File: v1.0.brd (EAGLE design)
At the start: 160 x 100 mm, 106 parts, among them J1 DC-044-A, J2 MICROSD-9P, J3 2p-2.54, J4 2p-2.54, Q1 SI4532ADY, Q3 6pF@32.7680kHz, U1 MCP23017-E/SO, U10 74HC139N, U2 MCP79412-I/SN, U3 LOPY, U4 GROVE_DC&DC, U5 LM1085IT-5.0, U6 FT232RL-SSOP28, U7 2x14p-2.54, U8 FT232RL-SSOP28, U9 SP483ECN-L, X1 JST-XH-05-PIN-ROUND-PAD, X10 JST-XH-07-PIN-ROUND-PAD, X11 JST-XH-07-PIN-ROUND-PAD, X12 JST-XH-07-PIN-ROUND-PAD, X13 JST-XH-05-PIN-ROUND-PAD, X14 JST-XH-05-PIN-ROUND-PAD, X15 JST-XH-05-PIN-ROUND-PAD, X16 JST-XH-05-PIN-ROUND-PAD, X17 JST-XH-05-PIN-ROUND-PAD, X18 JST-XH-05-PIN-ROUND-PAD, X19 JST-XH-05-PIN-ROUND-PAD, X2 JST-XH-05-PIN-ROUND-PAD, X20 JST-XH-05-PIN-ROUND-PAD, X21 JST-XH-05-PIN-ROUND-PAD, X22 JST-XH-05-PIN-ROUND-PAD, X23 JST-XH-05-PIN-ROUND-PAD, X3 JST-XH-05-PIN-ROUND-PAD, X4 JST-XH-07-PIN-ROUND-PAD, X5 JST-XH-07-PIN-ROUND-PAD, X6 JST-XH-07-PIN-ROUND-PAD, X7 JST-XH-07-PIN-ROUND-PAD, X8 JST-XH-07-PIN-ROUND-PAD, X9 JST-XH-07-PIN-ROUND-PAD

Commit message: adc sockets
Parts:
- added X24, X25, X26, X27: JST-XH-07-PIN-ROUND-PAD, Rembrandt Electronics - JST XH Connectors v1-0 2:JST-XH-07-PACKAGE-ROUND-PAD
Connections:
- removed net N$13: U$1.2
- removed net N$14: U$1.3
- removed net N$15: U$1.4
- removed net N$16: U$1.11
- removed net N$19: U$1.1
- removed net N$22: U$2.1
- removed net N$24: U$1.12
- removed net N$26: U$1.13
- removed net N$27: U$1.14
- removed net N$35: U$2.2
- removed net N$36: U$2.3
- removed net N$39: U$2.4
- removed net N$40: U$2.11
- removed net N$41: U$2.12
- removed net N$42: U$2.13
- removed net N$44: U$2.14
- new net ADC1+: U$1.1, X27.4
- new net ADC1-: U$1.2, X27.5
- new net ADC2+: U$1.3, X27.6
- new net ADC2-: U$1.4, X27.7
- new net ADC3+: U$1.11, X24.4
- new net ADC3-: U$1.12, X24.5
- new net ADC4+: U$1.13, X24.6
- new net ADC4-: U$1.14, X24.7
- new net ADC5+: U$2.1, X25.4
- new net ADC5-: U$2.2, X25.5
- new net ADC6+: U$2.3, X25.6
- new net ADC6-: U$2.4, X25.7
- new net ADC7+: U$2.11, X26.4
- new net ADC7-: U$2.12, X26.5
- new net ADC8+: U$2.13, X26.6
- new net ADC8-: U$2.14, X26.7
- net 3V3_SMOOTH: now also X24.2, X25.2, X26.2, X27.2
- net GND: now also X24.3, X25.3, X26.3, X27.3
- net PI_5V: now also X24.1, X25.1, X26.1, X27.1
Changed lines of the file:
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@@
 <element name="X21" library="Rembrandt Electronics - JST XH Connectors v1-0 2" package="JST-XH-05-PACKAGE-ROUND-PAD" value="JST-XH-05-PIN-ROUND-PAD" x="-134.62" y="-118.11"/>
 <element name="X22" library="Rembrandt Electronics - JST XH Connectors v1-0 2" package="JST-XH-05-PACKAGE-ROUND-PAD" value="JST-XH-05-PIN-ROUND-PAD" x="-134.62" y="-133.35"/>
+<element name="X27" library="Rembrandt Electronics - JST XH Connectors v1-0 2" package="JST-XH-07-PACKAGE-ROUND-PAD" value="JST-XH-07-PIN-ROUND-PAD" x="-132.08" y="-194.31"/>
+<element name="X24" library="Rembrandt Electronics - JST XH Connectors v1-0 2" package="JST-XH-07-PACKAGE-ROUND-PAD" value="JST-XH-07-PIN-ROUND-PAD" x="-132.08" y="-209.55"/>
+<element name="X25" library="Rembrandt Electronics - JST XH Connectors v1-0 2" package="JST-XH-07-PACKAGE-ROUND-PAD" value="JST-XH-07-PIN-ROUND-PAD" x="-132.08" y="-224.79"/>
+<element name="X26" library="Rembrandt Electronics - JST XH Connectors v1-0 2" package="JST-XH-07-PACKAGE-ROUND-PAD" value="JST-XH-07-PIN-ROUND-PAD" x="-132.08" y="-240.03"/>
 </elements>
 <signals>
@@
 <contactref element="X21" pad="3"/>
 <contactref element="X22" pad="3"/>
+<contactref element="X27" pad="3"/>
+<contactref element="X24" pad="3"/>
+<contactref element="X25" pad="3"/>
+<contactref element="X26" pad="3"/>
 <wire x1="-134.62" y1="-102.87" x2="-134.62" y2="-118.11" width="0" layer="19" extent="1-1"/>
 <wire x1="-134.62" y1="-87.63" x2="-134.62" y2="-102.87" width="0" layer="19" extent="1-1"/>
@@
 <wire x1="-15.24" y1="158.369" x2="-15.24" y2="163.322" width="0" layer="19" extent="1-1"/>
 <wire x1="-86.36" y1="156.718" x2="-106.68" y2="155.448" width="0" layer="19" extent="1-1"/>
+<wire x1="-134.62" y1="-194.31" x2="-134.62" y2="-133.35" width="0" layer="19" extent="1-1"/>
+<wire x1="-134.62" y1="-209.55" x2="-134.62" y2="-194.31" width="0" layer="19" extent="1-1"/>
+<wire x1="-134.62" y1="-224.79" x2="-134.62" y2="-209.55" width="0" layer="19" extent="1-1"/>
+<wire x1="-134.62" y1="-240.03" x2="-134.62" y2="-224.79" width="0" layer="19" extent="1-1"/>
 </signal>
 <signal name="+3V3">
@@
 <contactref element="X22" pad="1"/>
 <contactref element="X23" pad="1"/>
+<contactref element="X27" pad="1"/>
+<contactref element="X24" pad="1"/>
+<contactref element="X25" pad="1"/>
+<contactref element="X26" pad="1"/>
 <wire x1="-139.7" y1="-87.63" x2="-139.7" y2="-102.87" width="0" layer="19" extent="1-1"/>
 <wire x1="-139.7" y1="-72.39" x2="-139.7" y2="-87.63" width="0" layer="19" extent="1-1"/>
@@
 <wire x1="-40.7162" y1="93.345" x2="-30.48" y2="116.84" width="0" layer="19" extent="1-1"/>
 <wire x1="-20.32" y1="156.591" x2="-45.72" y2="161.798" width="0" layer="19" extent="1-1"/>
+<wire x1="-139.7" y1="-194.31" x2="-139.7" y2="-133.35" width="0" layer="19" extent="1-1"/>
+<wire x1="-139.7" y1="-209.55" x2="-139.7" y2="-194.31" width="0" layer="19" extent="1-1"/>
+<wire x1="-139.7" y1="-224.79" x2="-139.7" y2="-209.55" width="0" layer="19" extent="1-1"/>
+<wire x1="-139.7" y1="-240.03" x2="-139.7" y2="-224.79" width="0" layer="19" extent="1-1"/>
 </signal>
 <signal name="N$1">
@@
 <contactref element="X22" pad="2"/>
 <contactref element="X23" pad="2"/>
+<contactref element="X27" pad="2"/>
+<contactref element="X24" pad="2"/>
+<contactref element="X25" pad="2"/>
+<contactref element="X26" pad="2"/>
 <wire x1="-137.16" y1="-87.63" x2="-137.16" y2="-102.87" width="0" layer="19" extent="1-1"/>
 <wire x1="-137.16" y1="-72.39" x2="-137.16" y2="-87.63" width="0" layer="19" extent="1-1"/>
@@
 <wire x1="-137.16" y1="-118.11" x2="-137.16" y2="-102.87" width="0" layer="19" extent="1-1"/>
 <wire x1="-137.16" y1="-133.35" x2="-137.16" y2="-118.11" width="0" layer="19" extent="1-1"/>
+<wire x1="-137.16" y1="-194.31" x2="-137.16" y2="-133.35" width="0" layer="19" extent="1-1"/>
+<wire x1="-137.16" y1="-209.55" x2="-137.16" y2="-194.31" width="0" layer="19" extent="1-1"/>
+<wire x1="-137.16" y1="-224.79" x2="-137.16" y2="-209.55" width="0" layer="19" extent="1-1"/>
+<wire x1="-137.16" y1="-240.03" x2="-137.16" y2="-224.79" width="0" layer="19" extent="1-1"/>
 <wire x1="-120.65" y1="104.14" x2="-137.16" y2="-11.43" width="0" layer="19" extent="1-1"/>
 <wire x1="-119.38" y1="116.84" x2="-120.65" y2="104.14" width="0" layer="19" extent="1-1"/>
@@
 <wire x1="-104.14" y1="143.002" x2="-17.145" y2="102.81" width="0" layer="19" extent="1-1"/>
 </signal>
-<signal name="N$13">
+<signal name="ADC1-">
 <contactref element="U$1" pad="2"/>
-</signal>
-<signal name="N$14">
+<contactref element="X27" pad="5"/>
+<wire x1="-109.0422" y1="71.12" x2="-129.54" y2="-194.31" width="0" layer="19" extent="1-1"/>
+</signal>
+<signal name="ADC2+">
 <contactref element="U$1" pad="3"/>
-</signal>
-<signal name="N$15">
+<contactref element="X27" pad="6"/>
+<wire x1="-109.0422" y1="69.85" x2="-127" y2="-194.31" width="0" layer="19" extent="1-1"/>
+</signal>
+<signal name="ADC2-">
 <contactref element="U$1" pad="4"/>
-</signal>
-<signal name="N$16">
+<contactref element="X27" pad="7"/>
+<wire x1="-109.0422" y1="68.58" x2="-124.46" y2="-194.31" width="0" layer="19" extent="1-1"/>
+</signal>
+<signal name="ADC3+">
 <contactref element="U$1" pad="11"/>
+<contactref element="X24" pad="4"/>
+<wire x1="-104.3178" y1="68.58" x2="-132.08" y2="-209.55" width="0" layer="19" extent="1-1"/>
 </signal>
 <signal name="+3V3_SMOOTH">
@@
 <wire x1="-109.0422" y1="66.04" x2="-130.6322" y2="66.04" width="0" layer="19" extent="1-1"/>
 </signal>
-<signal name="N$19">
-<contactref element="U$1" pad="1"/>
-</signal>
-<signal name="N$24">
+<signal name="ADC3-">
 <contactref element="U$1" pad="12"/>
-</signal>
-<signal name="N$26">
+<contactref element="X24" pad="5"/>
+<wire x1="-104.3178" y1="69.85" x2="-129.54" y2="-209.55" width="0" layer="19" extent="1-1"/>
+</signal>
+<signal name="ADC4+">
 <contactref element="U$1" pad="13"/>
-</signal>
-<signal name="N$27">
+<contactref element="X24" pad="6"/>
+<wire x1="-104.3178" y1="71.12" x2="-127" y2="-209.55" width="0" layer="19" extent="1-1"/>
+</signal>
+<signal name="ADC4-">
 <contactref element="U$1" pad="14"/>
-</signal>
-<signal name="N$22">
+<contactref element="X24" pad="7"/>
+<wire x1="-104.3178" y1="72.39" x2="-124.46" y2="-209.55" width="0" layer="19" extent="1-1"/>
+</signal>
+<signal name="ADC5+">
 <contactref element="U$2" pad="1"/>
-</signal>
-<signal name="N$35">
+<contactref element="X25" pad="4"/>
+<wire x1="-130.6322" y1="72.39" x2="-132.08" y2="-224.79" width="0" layer="19" extent="1-1"/>
+</signal>
+<signal name="ADC5-">
 <contactref element="U$2" pad="2"/>
-</signal>
-<signal name="N$36">
+<contactref element="X25" pad="5"/>
+<wire x1="-130.6322" y1="71.12" x2="-129.54" y2="-224.79" width="0" layer="19" extent="1-1"/>
+</signal>
+<signal name="ADC6+">
 <contactref element="U$2" pad="3"/>
-</signal>
-<signal name="N$39">
+<contactref element="X25" pad="6"/>
+<wire x1="-130.6322" y1="69.85" x2="-127" y2="-224.79" width="0" layer="19" extent="1-1"/>
+</signal>
+<signal name="ADC6-">
 <contactref element="U$2" pad="4"/>
-</signal>
-<signal name="N$40">
+<contactref element="X25" pad="7"/>
+<wire x1="-130.6322" y1="68.58" x2="-124.46" y2="-224.79" width="0" layer="19" extent="1-1"/>
+</signal>
+<signal name="ADC7+">
 <contactref element="U$2" pad="11"/>
-</signal>
-<signal name="N$41">
-<contactref element="U$2" pad="12"/>
-</signal>
-<signal name="N$42">
+<contactref element="X26" pad="4"/>
+<wire x1="-125.9078" y1="68.58" x2="-132.08" y2="-240.03" width="0" layer="19" extent="1-1"/>
+</signal>
+<signal name="ADC8+">
 <contactref element="U$2" pad="13"/>
-</signal>
-<signal name="N$44">
+<contactref element="X26" pad="6"/>
+<wire x1="-125.9078" y1="71.12" x2="-127" y2="-240.03" width="0" layer="19" extent="1-1"/>
+</signal>
+<signal name="ADC8-">
 <contactref element="U$2" pad="14"/>
+<contactref element="X26" pad="7"/>
+<wire x1="-125.9078" y1="72.39" x2="-124.46" y2="-240.03" width="0" layer="19" extent="1-1"/>
 </signal>
 <signal name="N$23">
@@
 <wire x1="-45.6438" y1="92.075" x2="-64.355" y2="86.545" width="0" layer="19" extent="1-1"/>
 </signal>
+<signal name="ADC7-">
+<contactref element="X26" pad="5"/>
+<contactref element="U$2" pad="12"/>
+<wire x1="-125.9078" y1="69.85" x2="-129.54" y2="-240.03" width="0" layer="19" extent="1-1"/>
+</signal>
+<signal name="ADC1+">
+<contactref element="U$1" pad="1"/>
+<contactref element="X27" pad="4"/>
+<wire x1="-109.0422" y1="72.39" x2="-132.08" y2="-194.31" width="0" layer="19" extent="1-1"/>
+</signal>
 </signals>

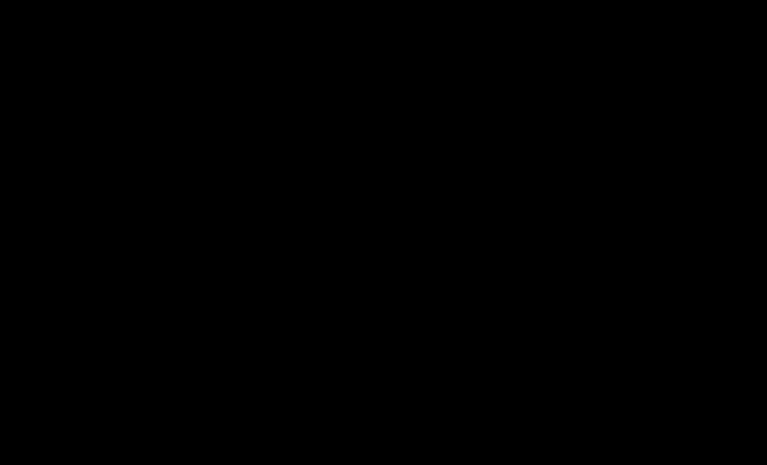
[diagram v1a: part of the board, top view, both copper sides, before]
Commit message: changed back to +5V - has LDO on it - and added RS485 socket
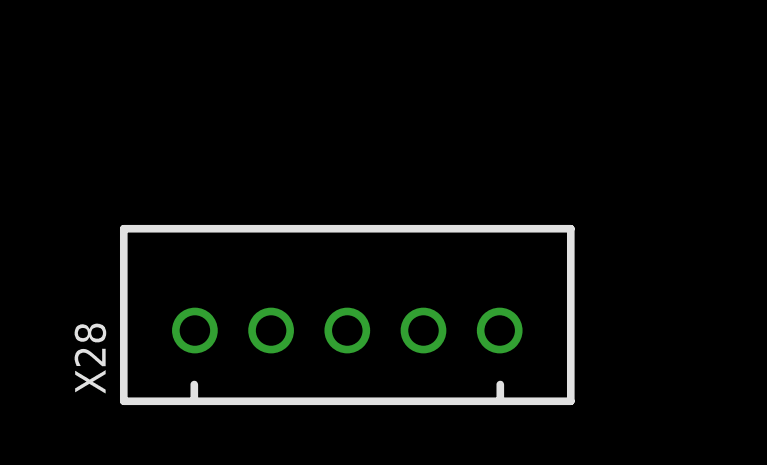
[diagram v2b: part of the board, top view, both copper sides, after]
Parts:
- added X28: JST-XH-05-PIN-ROUND-PAD, Rembrandt Electronics - JST XH Connectors v1-0 2:JST-XH-05-PACKAGE-ROUND-PAD
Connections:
- net +5V: now also X10.1, X11.1, X12.1, X13.1, X14.1, X15.1, X16.1, X17.1, X18.1, X19.1, X20.1, X21.1, X22.1, X23.1, X24.1, X25.1, X26.1, X27.1, X28.1, X5.1, X6.1, X7.1, X8.1, X9.1
- net 3V3_SMOOTH: now also X28.2
- net GND: now also X28.3
- net PI_5V: no longer X10.1, X11.1, X12.1, X13.1, X14.1, X15.1, X16.1, X17.1, X18.1, X19.1, X20.1, X21.1, X22.1, X23.1, X24.1, X25.1, X26.1, X27.1, X5.1, X6.1, X7.1, X8.1, X9.1
- net RS485_A: now also X28.4
- net RS485_B: now also X28.5

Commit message: zener diode
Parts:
- added U11: BZX84C30, Diodes_Inc_By_element14_Batch_1:SOT91P240X110-3N
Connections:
- net +24V: now also U11.1
- net GND: now also U11.3
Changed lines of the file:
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@@
 <element name="X26" library="Rembrandt Electronics - JST XH Connectors v1-0 2" package="JST-XH-07-PACKAGE-ROUND-PAD" value="JST-XH-07-PIN-ROUND-PAD" x="-132.08" y="-240.03"/>
 <element name="X28" library="Rembrandt Electronics - JST XH Connectors v1-0 2" package="JST-XH-05-PACKAGE-ROUND-PAD" value="JST-XH-05-PIN-ROUND-PAD" x="-134.62" y="-255.27"/>
+<element name="U11" library="Diodes_Inc_By_element14_Batch_1" package="SOT91P240X110-3N" value="BZX84C30" x="-143.51" y="-269.24">
+<attribute name="MPN" value="BZX84C30" x="-143.51" y="-269.24" size="1.778" layer="27" display="off"/>
+<attribute name="OC_FARNELL" value="1902456" x="-143.51" y="-269.24" size="1.778" layer="27" display="off"/>
+<attribute name="OC_NEWARK" value="-" x="-143.51" y="-269.24" size="1.778" layer="27" display="off"/>
+<attribute name="PACKAGE" value="SOT-23-3" x="-143.51" y="-269.24" size="1.778" layer="27" display="off"/>
+<attribute name="SUPPLIER" value="DIODES INC." x="-143.51" y="-269.24" size="1.778" layer="27" display="off"/>
+</element>
 </elements>
 <signals>
@@
 <contactref element="X26" pad="3"/>
 <contactref element="X28" pad="3"/>
+<contactref element="U11" pad="3"/>
 <wire x1="-134.62" y1="-102.87" x2="-134.62" y2="-118.11" width="0" layer="19" extent="1-1"/>
 <wire x1="-134.62" y1="-87.63" x2="-134.62" y2="-102.87" width="0" layer="19" extent="1-1"/>
@@
 <wire x1="-134.62" y1="-240.03" x2="-134.62" y2="-224.79" width="0" layer="19" extent="1-1"/>
 <wire x1="-134.62" y1="-255.27" x2="-134.62" y2="-240.03" width="0" layer="19" extent="1-1"/>
+<wire x1="-142.494" y1="-269.24" x2="-134.62" y2="-255.27" width="0" layer="19" extent="1-1"/>
 </signal>
 <signal name="+3V3">
@@
 <contactref element="U4" pad="P$1"/>
 <contactref element="R5" pad="2"/>
-<wire x1="-95.58" y1="143.51" x2="-40.64" y2="156.718" width="0" layer="19" extent="1-1"/>
-<wire x1="-73.66" y1="74.93" x2="-95.58" y2="143.51" width="0" layer="19" extent="1-1"/>
-<wire x1="-73.66" y1="72.39" x2="-73.66" y2="74.93" width="0" layer="19" extent="1-1"/>
+<contactref element="U11" pad="1"/>
+<wire x1="-73.66" y1="72.39" x2="-144.526" y2="-268.3256" width="0" layer="19" extent="1-1"/>
+<wire x1="-73.66" y1="74.93" x2="-73.66" y2="72.39" width="0" layer="19" extent="1-1"/>
+<wire x1="-95.58" y1="143.51" x2="-73.66" y2="74.93" width="0" layer="19" extent="1-1"/>
+<wire x1="-40.64" y1="156.718" x2="-95.58" y2="143.51" width="0" layer="19" extent="1-1"/>
 </signal>
 <signal name="3V3_SMOOTH">

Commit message: polyfuses
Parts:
- added F10, F100, F101, F102, F103, F104, F105, F106, F107, F108, F109, F11, F110, F111, F112, F113, F114, F115, F116, F117, F118, F119, F12, F120, F121, F122, F123, F13, F14, F15, F16, F17, F18, F19, F2, F20, F21, F22, F23, F24, F25, F26, F27, F28, F29, F3, F30, F31, F32, F33, F34, F35, F36, F37, F38, F39, F4, F40, F41, F42, F43, F44, F45, F46, F47, F48, F49, F5, F50, F51, F52, F53, F54, F55, F56, F57, F58, F59, F6, F60, F61, F62, F63, F64, F65, F66, F67, F68, F69, F7, F70, F71, F72, F73, F74, F75, F76, F77, F78, F79, F8, F80, F81, F82, F83, F84, F85, F86, F87, F88, F89, F9, F90, F91, F92, F93, F94, F95, F96, F97, F98, F99: SMD1206R500SF, Seeed-Fuse:F1206
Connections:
- new net N$12: F109.1, U1.22
- new net N$13: F110.1, U1.23
- new net N$14: F111.1, U1.24
- new net N$15: F112.1, U1.25
- new net N$16: F113.1, U1.26
- new net N$19: F114.1, U1.27
- new net N$2: F106.1, U1.19
- new net N$22: F115.1, U1.28
- new net N$24: F116.1, U1.1
- new net N$26: F117.1, U1.2
- new net N$27: F118.1, U1.3
- new net N$3: F107.1, U1.20
- new net N$35: F119.1, U1.4
- new net N$36: F120.1, U1.5
- new net N$37: F121.1, U1.6
- new net N$39: F122.1, U1.7
- new net N$40: F123.1, U1.8
- new net N$8: F108.1, U1.21
- net ADC1+: now also F54.2
- net ADC1-: now also F55.2
- net ADC2+: now also F56.2
- net ADC2-: now also F57.2
- net ADC3+: now also F58.2
- net ADC3-: now also F59.2
- net ADC4+: now also F60.2
- net ADC4-: now also F61.2
- net ADC5+: now also F62.2
- net ADC5-: now also F63.2
- net ADC6+: now also F64.2
- net ADC6-: now also F65.2
- net ADC7+: now also F66.2
- net ADC7-: now also F67.2
- net ADC8+: now also F68.2
- net ADC8-: now also F69.2
- net LOPY_CS: now also F74.2
- net LOPY_MISO: now also F76.2
- net LOPY_MOSI: now also F77.2
- net LOPY_P13: now also F94.2, F95.1
- net LOPY_P14: now also F93.2, F96.1
- net LOPY_P15: now also F92.2, F97.1
- net LOPY_P16: now also F91.2, F98.1
- net LOPY_P17: now also F90.2, F99.1
- net LOPY_P18: now also F100.1, F89.2
- net LOPY_P19: now also F101.1, F88.2
- net LOPY_P20: now also F102.1, F87.2
- net LOPY_P21: now also F103.1, F86.2
- net LOPY_P22: now also F104.1, F85.2
- net LOPY_P23: now also F105.1, F84.2
- net LOPY_RX0: now also F83.2
- net LOPY_RX1: now also F81.2
- net LOPY_SCL/CLK: now also F75.2, F78.2
- net LOPY_SDA: now also F79.2
- net LOPY_TX0: now also F82.2
- net LOPY_TX1: now also F80.2
- net RPI_CS1: now also F28.2
- net RPI_CS2: now also F29.2
- net RPI_CS3: now also F33.2
- net RPI_CS4: now also F37.2
- net RPI_CS5: now also F41.2
- net RPI_CS6: now also F45.2
- net RPI_CS7: now also F49.2
- net RPI_CS8: now also F53.2
- net RS485_A: now also F72.2
- net RS485_B: now also F73.2
- net SCL_3V3: now also F11.2, F13.2, F15.2, F17.2, F19.2, F21.2, F3.2, F5.2, F6.2, F9.2
- net SDA_3V3: now also F10.2, F12.2, F14.2, F16.2, F18.2, F2.2, F20.2, F4.2, F7.2, F8.2
- net SPI_MISO: now also F23.2, F25.2, F30.2, F35.2, F38.2, F42.2, F47.2, F50.2
- net SPI_MOSI: now also F22.2, F26.2, F31.2, F34.2, F39.2, F43.2, F46.2, F51.2
- net SPI_SCLK: now also F24.2, F27.2, F32.2, F36.2, F40.2, F44.2, F48.2, F52.2
- net UART_RX: now also F70.2
- net UART_TDX: now also F71.2

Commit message: start of poly fuse tidy
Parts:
- removed F100, F101, F102, F103, F104, F105, F106, F107, F108, F109, F110, F111, F112, F113, F114, F115, F116, F117, F118, F119, F120, F121, F122, F123, F23, F24, F25, F26, F27, F28, F29, F30, F31, F32, F33, F34, F35, F36, F37, F38, F39, F40, F41, F42, F43, F44, F45, F46, F47, F48, F49, F50, F51, F52, F53, F54, F55, F56, F57, F58, F59, F60, F61, F62, F63, F64, F65, F66, F67, F68, F69, F70, F71, F72, F73, F84, F85, F86, F87, F88, F89, F90, F91, F92, F93, F94, F95, F96, F97, F98, F99: SMD1206R500SF, Seeed-Fuse:F1206
- removed X22: JST-XH-05-PIN-ROUND-PAD, Rembrandt Electronics - JST XH Connectors v1-0 2:JST-XH-05-PACKAGE-ROUND-PAD
- moved X21 863.9 mm to (-909.3, -500.4)
- moved X20 857.8 mm to (-909.3, -471.2)
- moved X19 851.9 mm to (-909.3, -442.0)
- moved X18 846.2 mm to (-909.3, -412.8)
- moved X17 840.6 mm to (-909.3, -383.5)
- moved X16 835.3 mm to (-909.3, -354.3)
- moved X15 830.2 mm to (-909.3, -325.1)
- moved X14 825.3 mm to (-909.3, -295.9)
- moved F6 743.1 mm to (-920.8, -284.5)
- moved F7 737.5 mm to (-920.8, -307.3)
- moved F8 731.5 mm to (-920.8, -313.7)
- moved F9 726.9 mm to (-920.8, -336.6)
- moved F10 721.2 mm to (-920.8, -342.9)
- moved F11 717.6 mm to (-920.8, -365.8)
- moved F12 712.1 mm to (-920.8, -372.1)
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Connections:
- new net N$41: F78.2, X1.1
- new net N$42: F79.2, X1.2
- new net N$43: F80.2, X2.1
- new net N$44: F81.2, X2.2
- new net N$45: F82.2, X3.1
- new net N$46: F4.2, X5.2
- new net N$47: F74.2, X4.1
- new net N$48: F8.2, X14.2
- new net N$49: F6.2, X13.2
- new net N$50: F10.2, X15.2
- new net N$51: F12.2, X16.2
- new net N$52: F14.2, X17.2
- new net N$53: F16.2, X18.2
- new net N$54: F18.2, X19.2
- new net N$55: F20.2, X20.2
- new net N$56: F22.2, X21.2
- net +5V: now also F11.1, F11.2, F13.1, F13.2, F15.1, F15.2, F17.1, F17.2, F19.1, F19.2, F21.1, F21.2, F3.1, F5.1, F5.2, F7.1, F7.2, F74.1, F76.1, F76.2, F78.1, F80.1, F82.1, F9.1, F9.2; no longer X1.1, X2.1, X22.1, X3.1, X4.1, X5.1
- net 3V3_SMOOTH: now also F4.1; no longer X13.2, X14.2, X15.2, X16.2, X17.2, X18.2, X19.2, X20.2, X21.2, X22.2, X5.2
- net ADC1+: no longer F54.2
- net ADC1-: no longer F55.2
- net ADC2+: no longer F56.2
- net ADC2-: no longer F57.2
- net ADC3+: no longer F58.2
- net ADC3-: no longer F59.2
- net ADC4+: no longer F60.2
- net ADC4-: no longer F61.2
- net ADC5+: no longer F62.2
- net ADC5-: no longer F63.2
- net ADC6+: no longer F64.2
- net ADC6-: no longer F65.2
- net ADC7+: no longer F66.2
- net ADC7-: no longer F67.2
- net ADC8+: no longer F68.2
- net ADC8-: no longer F69.2
- net GND: no longer X22.3
- net LOPY_3V3: now also F10.1, F12.1, F14.1, F16.1, F18.1, F20.1, F22.1, F6.1, F75.1, F75.2, F77.1, F77.2, F79.1, F8.1, F81.1, F83.1, F83.2; no longer X1.2, X2.2
- net LOPY_CS: no longer F74.2
- net LOPY_MISO: no longer F76.2
- net LOPY_MOSI: no longer F77.2
- net LOPY_P13: no longer F94.2, F95.1
- net LOPY_P14: no longer F93.2, F96.1
- net LOPY_P15: no longer F92.2, F97.1
- net LOPY_P16: no longer F91.2, F98.1
- net LOPY_P17: no longer F90.2, F99.1
- net LOPY_P18: no longer F100.1, F89.2
- net LOPY_P19: no longer F101.1, F88.2
- net LOPY_P20: no longer F102.1, F87.2
- net LOPY_P21: no longer F103.1, F86.2
- net LOPY_P22: no longer F104.1, F85.2
- net LOPY_P23: no longer F105.1, F84.2
- net LOPY_RX0: no longer F83.2
- net LOPY_RX1: no longer F81.2
- net LOPY_SCL/CLK: no longer F75.2, F78.2
- net LOPY_SDA: no longer F79.2
- net LOPY_TX0: no longer F82.2
- net LOPY_TX1: no longer F80.2
- net N$12: no longer F109.1
- net N$13: no longer F110.1
- net N$14: no longer F111.1
- net N$15: no longer F112.1
- net N$16: no longer F113.1
- net N$19: no longer F114.1
- net N$2: no longer F106.1
- net N$22: no longer F115.1
- net N$24: no longer F116.1
- net N$26: no longer F117.1
- net N$27: no longer F118.1
- net N$3: no longer F107.1
- net N$35: no longer F119.1
- net N$36: no longer F120.1
- net N$37: no longer F121.1
- net N$39: no longer F122.1
- net N$40: no longer F123.1
- net N$8: no longer F108.1
- net RPI_CS1: no longer F28.2
- net RPI_CS2: no longer F29.2
- net RPI_CS3: no longer F33.2
- net RPI_CS4: no longer F37.2
- net RPI_CS5: no longer F41.2
- net RPI_CS6: no longer F45.2
- net RPI_CS7: no longer F49.2
- net RPI_CS8: no longer F53.2
- net RS485_A: no longer F72.2
- net RS485_B: no longer F73.2
- net SCL_3V3: no longer F11.2, F13.2, F15.2, F17.2, F19.2, F21.2, F3.2, F5.2, F6.2, F9.2, X22.5
- net SDA_3V3: no longer F10.2, F12.2, F14.2, F16.2, F18.2, F2.2, F20.2, F4.2, F7.2, F8.2, X22.4
- net SPI_MISO: no longer F23.2, F25.2, F30.2, F35.2, F38.2, F42.2, F47.2, F50.2
- net SPI_MOSI: no longer F22.2, F26.2, F31.2, F34.2, F39.2, F43.2, F46.2, F51.2
- net SPI_SCLK: no longer F24.2, F27.2, F32.2, F36.2, F40.2, F44.2, F48.2, F52.2
- net UART_RX: no longer F70.2
- net UART_TDX: no longer F71.2
